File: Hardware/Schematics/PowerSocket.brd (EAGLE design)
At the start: 100 x 47.6 mm, 74 parts, among them T1 BT138-V, T2 BT138-V, T3 BT138-V, T4 BT138-V, T5 BT138-V, T6 BT138-V

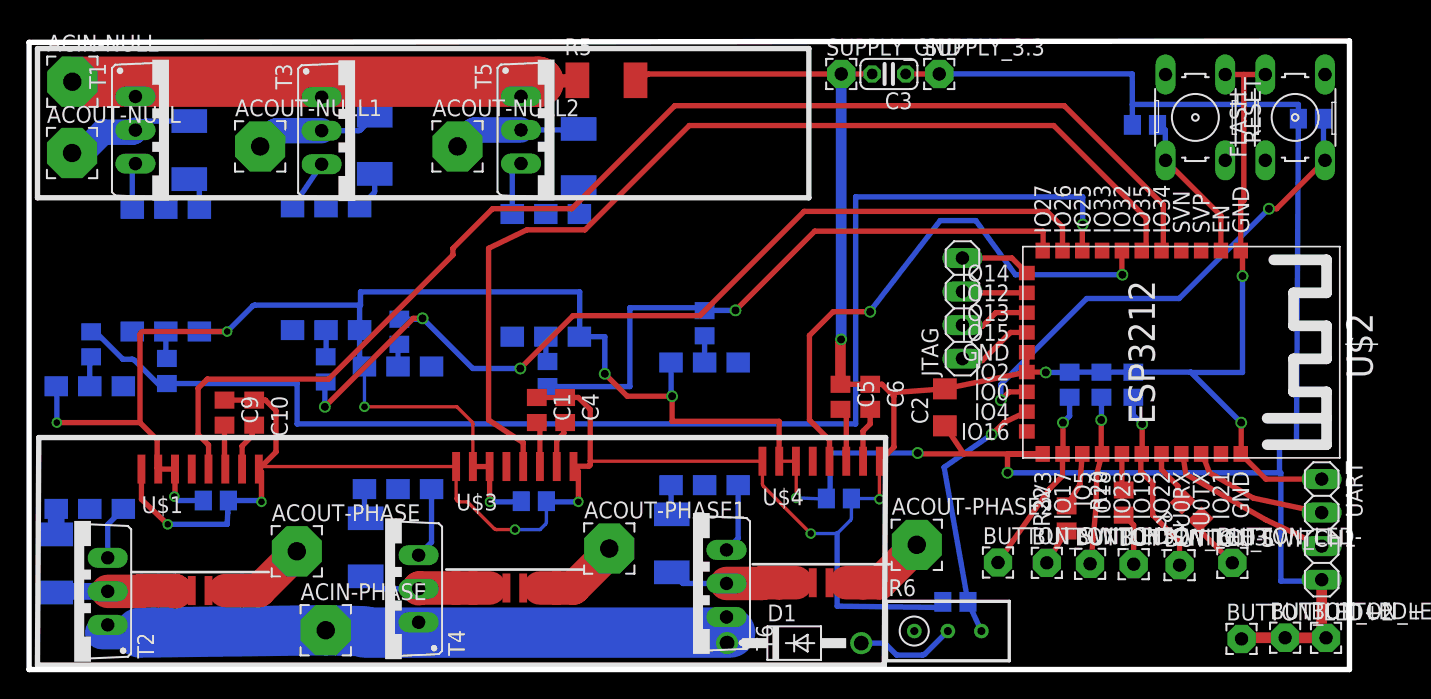
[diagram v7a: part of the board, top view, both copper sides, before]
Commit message: Added GND planes.
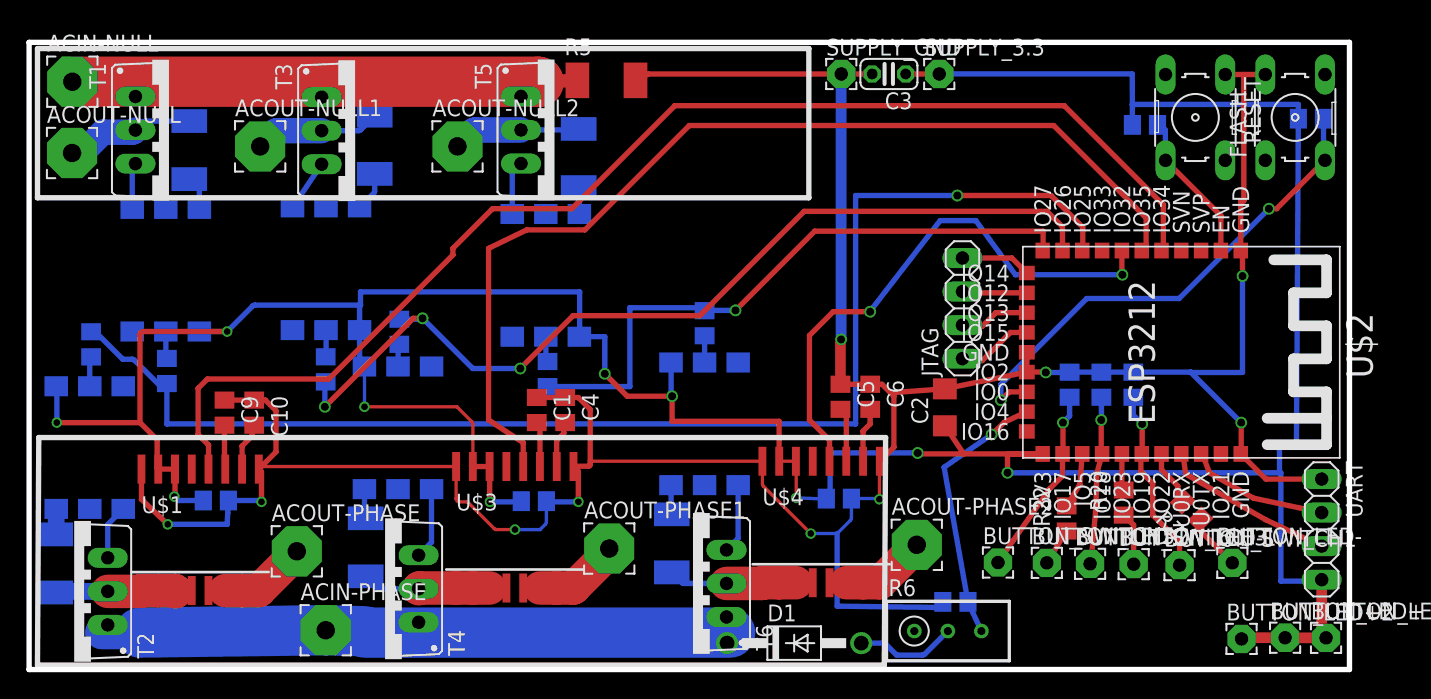
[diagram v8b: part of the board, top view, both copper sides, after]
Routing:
- net N$8: track 101.6 -> 100.3 mm
- added copper zone on layer 16, net GND
- added copper zone on layer 1, net N$37
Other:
- board size 100 x 47.6 mm -> 100 x 47.5 mm
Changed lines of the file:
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@@
 <plain>
 <wire x1="0" y1="1.1" x2="100" y2="1.1" width="0.4064" layer="20"/>
-<wire x1="100" y1="1.1" x2="100" y2="48.7" width="0.4064" layer="20"/>
-<wire x1="100" y1="48.7" x2="0" y2="48.6" width="0.4064" layer="20"/>
+<wire x1="100" y1="1.1" x2="100" y2="48.6" width="0.4064" layer="20"/>
+<wire x1="100" y1="48.6" x2="0" y2="48.6" width="0.4064" layer="20"/>
 <wire x1="0" y1="48.6" x2="0" y2="1.1" width="0.4064" layer="20"/>
 <wire x1="0.635" y1="1.435" x2="64.77" y2="1.435" width="0.4064" layer="21"/>
@@
 <wire x1="61.5" y1="26.1" x2="61.5" y2="46.195" width="0.8128" layer="16"/>
 <wire x1="61.5" y1="46.195" x2="61.51" y2="46.205" width="0.8128" layer="16"/>
+<polygon width="0.4064" layer="16" isolate="0.8128">
+<vertex x="0" y="1.2"/>
+<vertex x="0" y="48.6"/>
+<vertex x="100" y="48.6"/>
+<vertex x="100" y="48.5"/>
+<vertex x="100" y="1"/>
+<vertex x="0" y="1"/>
+</polygon>
 </signal>
 <signal name="VCC">
@@
 <wire x1="10.1" y1="22.4" x2="10.435" y2="22.4" width="0.4064" layer="16"/>
 <wire x1="10.435" y1="22.4" x2="10.435" y2="22.76" width="0.4064" layer="16"/>
-<wire x1="10.435" y1="22.76" x2="20.3" y2="22.76" width="0.4064" layer="16"/>
-<wire x1="20.3" y1="22.76" x2="20.3" y2="19.7" width="0.4064" layer="16"/>
-<wire x1="20.3" y1="19.7" x2="62.6" y2="19.7" width="0.4064" layer="16"/>
-<wire x1="62.6" y1="19.7" x2="62.6" y2="36.9" width="0.4064" layer="16"/>
-<wire x1="62.6" y1="36.9" x2="79.8" y2="36.9" width="0.4064" layer="16"/>
-<wire x1="79.8" y1="36.9" x2="79.8" y2="34.8" width="0.4064" layer="16"/>
-<via x="79.8" y="34.8" extent="1-16" drill="0.6" shape="square"/>
-<wire x1="79.8" y1="34.8" x2="79.765" y2="34.8" width="0.4064" layer="1"/>
-<wire x1="79.765" y1="34.8" x2="79.765" y2="32.83" width="0.4064" layer="1"/>
+<wire x1="10.435" y1="19.7" x2="62.6" y2="19.7" width="0.4064" layer="16"/>
+<wire x1="62.6" y1="19.7" x2="62.6" y2="37" width="0.4064" layer="16"/>
+<via x="70.3" y="37" extent="1-16" drill="0.6" shape="square"/>
+<wire x1="10.435" y1="22.76" x2="10.435" y2="19.7" width="0.4064" layer="16"/>
+<wire x1="62.6" y1="37" x2="70.3" y2="37" width="0.4064" layer="16"/>
+<wire x1="70.3" y1="37" x2="77.4" y2="37" width="0.4064" layer="1"/>
+<wire x1="77.4" y1="37" x2="79.8" y2="34.6" width="0.4064" layer="1"/>
+<wire x1="79.8" y1="34.6" x2="79.8" y2="32.865" width="0.4064" layer="1"/>
+<wire x1="79.8" y1="32.865" x2="79.765" y2="32.83" width="0.4064" layer="1"/>
 </signal>
 <signal name="N$12">
@@
 <contactref element="U$4" pad="13"/>
 </signal>
+<signal name="N$37">
+<polygon width="0.4064" layer="1" isolate="0.8128">
+<vertex x="100" y="1.1"/>
+<vertex x="0" y="1.1"/>
+<vertex x="0" y="48.6"/>
+<vertex x="100" y="48.6"/>
+</polygon>
+</signal>
 </signals>
